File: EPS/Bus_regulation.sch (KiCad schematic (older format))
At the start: 1 part

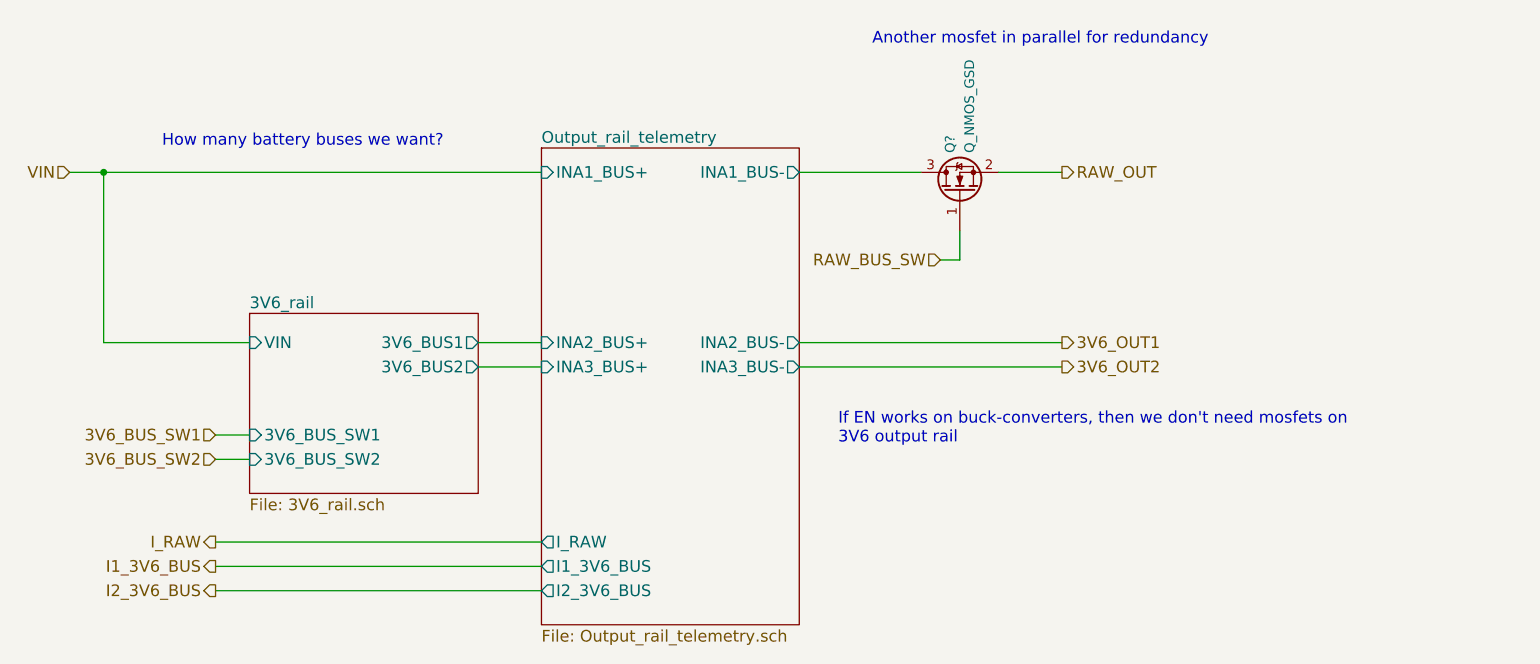
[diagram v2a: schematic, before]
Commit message: Finalized SCH (beta version) and started pcb
Capacitor banks might need to be reassigned to other locations.
No RBF pin on this SCH or PCB.
Battery gound deployment switch is fully mechanical (no mosfet switch on low side).
PCB of the prototype started. Main power converters and current measuring devices layed out.
SCH still requires ESD protection diodes!
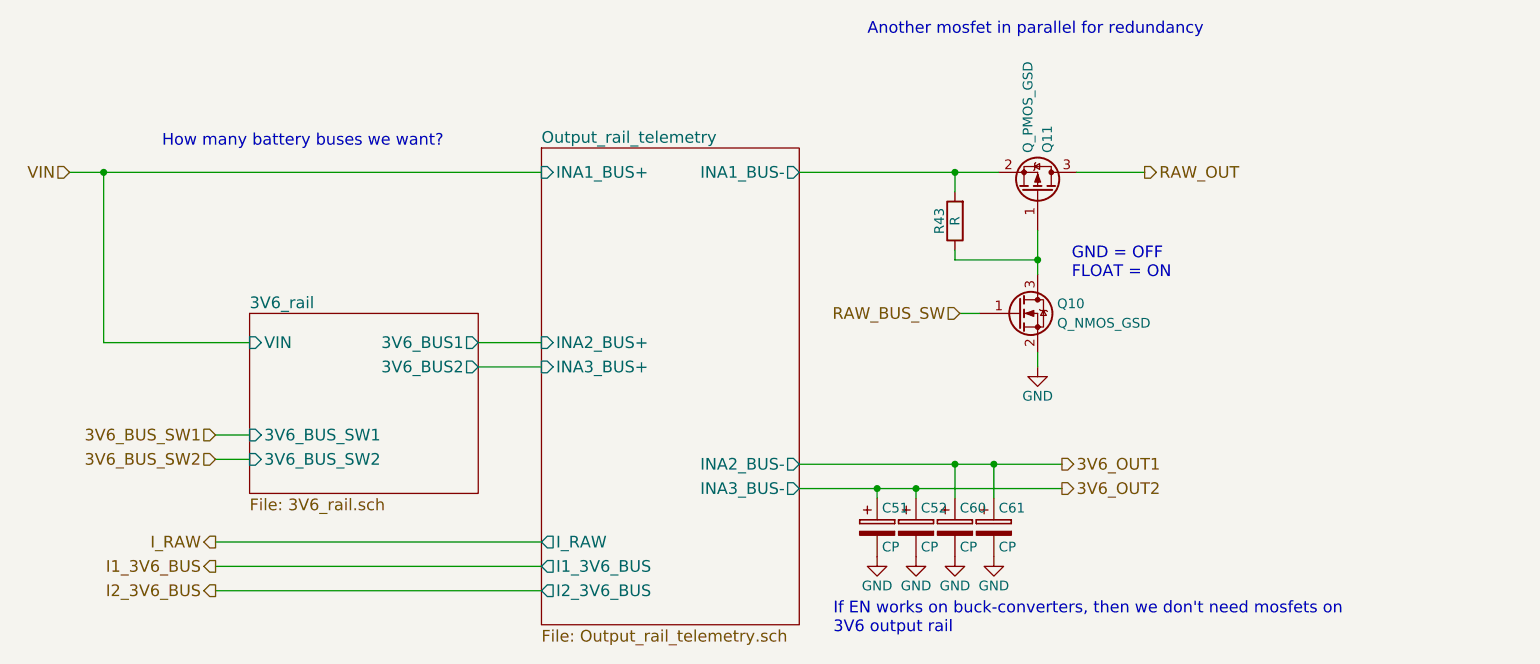
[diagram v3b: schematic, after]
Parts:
- removed Q?: Q_NMOS_GSD, symbol Q_NMOS_GSD
- added C51, C52, C60, C61: CP, Capacitors_Tantalum_SMD:CP_Tantalum_Case-C_EIA-6032-28_Reflow, symbol CP
- added Q10: Q_NMOS_GSD, TO_SOT_Packages_SMD:SOT-23, symbol Q_NMOS_GSD
- added Q11: Q_PMOS_GSD, TO_SOT_Packages_SMD:SOT-23, symbol Q_PMOS_GSD
- added R43: R, Resistors_SMD:R_0603, symbol R
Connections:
- net 3V6_OUT1: now also C60.1, C61.1
- net 3V6_OUT2: now also C51.1, C52.1
- net Output_rail_telemetry/INA1_BUS-: now also Q11.2 (S), R43.2
- net RAW_BUS_SW: now also Q10.1 (G)
- net RAW_OUT: now also Q11.3 (D)
- new net: Q10.3 (D), Q11.1 (G), R43.1
- new net GND: C51.2, C52.2, C60.2, C61.2, Q10.2 (S)
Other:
- note added: "GND = OFF\nFLOAT = ON"
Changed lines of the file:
@@
 $Descr A4 11693 8268
 encoding utf-8
-Sheet 10 14
+Sheet 9 14
 Title "Output regulation"
-Date "2018-02-15"
+Date "2018-02-22"
 Rev "R1"
 Comp ""
@@
 Text HLabel 3925 3725 0    60   Input ~ 0
 3V6_BUS_SW1
-Wire Wire Line
-	3925 3725 4100 3725
 Text HLabel 3925 3850 0    60   Input ~ 0
 3V6_BUS_SW2
-Wire Wire Line
-	3925 3850 4100 3850
 $Sheet
 S 5600 2250 1325 2450
@@
 F5 "I1_3V6_BUS" O L 5600 4400 60
 F6 "INA2_BUS+" I L 5600 3250 60
-F7 "INA2_BUS-" O R 6925 3250 60
-F8 "INA3_BUS-" O R 6925 3375 60
+F7 "INA2_BUS-" O R 6925 3875 60
+F8 "INA3_BUS-" O R 6925 4000 60
 F9 "INA3_BUS+" I L 5600 3375 60
 F10 "I2_3V6_BUS" O L 5600 4525 60
 $EndSheet
-Wire Wire Line
-	5600 2375 3175 2375
-Wire Wire Line
-	3350 2375 3350 3250
-Wire Wire Line
-	3350 3250 4100 3250
-Connection ~ 3350 2375
-Wire Wire Line
-	5275 3250 5600 3250
-Wire Wire Line
-	5275 3375 5600 3375
 Text HLabel 3925 4275 0    60   Output ~ 0
 I_RAW
-Wire Wire Line
-	3925 4275 5600 4275
 Text HLabel 3925 4400 0    60   Output ~ 0
 I1_3V6_BUS
-Wire Wire Line
-	3925 4400 5600 4400
 Text HLabel 3925 4525 0    60   Output ~ 0
 I2_3V6_BUS
-Wire Wire Line
-	3925 4525 5600 4525
-$Comp
-L Q_NMOS_GSD Q?
-U 1 1 5A9C3DA7
-P 7750 2475
-F 0 "Q?" H 7950 2525 50  0000 L CNN
-F 1 "Q_NMOS_GSD" H 7950 2425 50  0000 L CNN
-F 2 "" H 7950 2575 50  0001 C CNN
-F 3 "" H 7750 2475 50  0001 C CNN
-	1    7750 2475
-	0    -1   -1   0
-$EndComp
-Wire Wire Line
-	7550 2375 6925 2375
-Text HLabel 8275 2375 2    60   Output ~ 0
+Text HLabel 8700 2375 2    60   Output ~ 0
 RAW_OUT
-Wire Wire Line
-	8275 2375 7950 2375
-Text HLabel 8275 3250 2    60   Output ~ 0
+Text HLabel 8275 3875 2    60   Output ~ 0
 3V6_OUT1
-Text HLabel 8275 3375 2    60   Output ~ 0
+Text HLabel 8275 4000 2    60   Output ~ 0
 3V6_OUT2
-Wire Wire Line
-	8275 3375 6925 3375
-Wire Wire Line
-	6925 3250 8275 3250
-Text HLabel 7650 2825 0    60   Input ~ 0
+Text HLabel 7750 3100 0    60   Input ~ 0
 RAW_BUS_SW
-Wire Wire Line
-	7650 2825 7750 2825
-Wire Wire Line
-	7750 2825 7750 2675
-Text Notes 7125 3775 0    60   ~ 0
+Text Notes 7100 4750 0    60   ~ 0
 If EN works on buck-converters, then we don't need mosfets on\n3V6 output rail
-Text Notes 7300 1725 0    60   ~ 0
+Text Notes 7275 1675 0    60   ~ 0
 Another mosfet in parallel for redundancy
 Text Notes 3650 2250 0    60   ~ 0
 How many battery buses we want?
+$Comp
+L R R43
+U 1 1 5A9F980B
+P 7725 2625
+F 0 "R43" V 7805 2625 50  0000 C CNN
+F 1 "R" V 7725 2625 50  0000 C CNN
+F 2 "Resistors_SMD:R_0603" V 7655 2625 50  0001 C CNN
+F 3 "" H 7725 2625 50  0001 C CNN
+	1    7725 2625
+	-1   0    0    1
+$EndComp
+$Comp
+L Q_NMOS_GSD Q10
+U 1 1 5A9F9825
+P 8050 3100
+F 0 "Q10" H 8250 3150 50  0000 L CNN
+F 1 "Q_NMOS_GSD" H 8250 3050 50  0000 L CNN
+F 2 "TO_SOT_Packages_SMD:SOT-23" H 8250 3200 50  0001 C CNN
+F 3 "" H 8050 3100 50  0001 C CNN
+	1    8050 3100
+	1    0    0    -1
+$EndComp
+$Comp
+L GND #PWR0110
+U 1 1 5A9F982C
+P 8150 3375
+F 0 "#PWR0110" H 8150 3125 50  0001 C CNN
+F 1 "GND" H 8150 3225 50  0000 C CNN
+F 2 "" H 8150 3375 50  0001 C CNN
+F 3 "" H 8150 3375 50  0001 C CNN
+	1    8150 3375
+	1    0    0    -1
+$EndComp
+Text Notes 8325 2925 0    60   ~ 0
+GND = OFF\nFLOAT = ON
+$Comp
+L Q_PMOS_GSD Q11
+U 1 1 5A9FD422
+P 8150 2475
+F 0 "Q11" H 8350 2525 50  0000 L CNN
+F 1 "Q_PMOS_GSD" H 8350 2425 50  0000 L CNN
+F 2 "TO_SOT_Packages_SMD:SOT-23" H 8350 2575 50  0001 C CNN
+F 3 "" H 8150 2475 50  0001 C CNN
+	1    8150 2475
+	0    1    -1   0
+$EndComp
+Wire Wire Line
+	3925 3725 4100 3725
+Wire Wire Line
+	3925 3850 4100 3850
+Wire Wire Line
+	3175 2375 5600 2375
+Wire Wire Line
+	3350 2375 3350 3250
+Wire Wire Line
+	3350 3250 4100 3250
+Connection ~ 3350 2375
+Wire Wire Line
+	5275 3250 5600 3250
+Wire Wire Line
+	5275 3375 5600 3375
+Wire Wire Line
+	3925 4275 5600 4275
+Wire Wire Line
+	3925 4400 5600 4400
+Wire Wire Line
+	3925 4525 5600 4525
+Wire Wire Line
+	6925 2375 7950 2375
+Wire Wire Line
+	8350 2375 8700 2375
+Wire Wire Line
+	7725 2475 7725 2375
+Connection ~ 7725 2375
+Wire Wire Line
+	7725 2775 7725 2825
+Wire Wire Line
+	7725 2825 8150 2825
+Wire Wire Line
+	8150 2675 8150 2900
+Connection ~ 8150 2825
+Wire Wire Line
+	8150 3375 8150 3300
+Wire Wire Line
+	7850 3100 7750 3100
+Wire Wire Line
+	6925 3875 8275 3875
+Wire Wire Line
+	8275 4000 6925 4000
+$Comp
+L CP C52
+U 1 1 5A96ADC2
+P 7525 4200
+F 0 "C52" H 7550 4300 50  0000 L CNN
+F 1 "CP" H 7550 4100 50  0000 L CNN
+F 2 "Capacitors_Tantalum_SMD:CP_Tantalum_Case-C_EIA-6032-28_Reflow" H 7563 4050 50  0001 C CNN
+F 3 "" H 7525 4200 50  0001 C CNN
+	1    7525 4200
+	1    0    0    -1
+$EndComp
+$Comp
+L CP C51
+U 1 1 5A96AE4D
+P 7325 4200
+F 0 "C51" H 7350 4300 50  0000 L CNN
+F 1 "CP" H 7350 4100 50  0000 L CNN
+F 2 "Capacitors_Tantalum_SMD:CP_Tantalum_Case-C_EIA-6032-28_Reflow" H 7363 4050 50  0001 C CNN
+F 3 "" H 7325 4200 50  0001 C CNN
+	1    7325 4200
+	1    0    0    -1
+$EndComp
+$Comp
+L CP C60
+U 1 1 5A96AF69
+P 7725 4200
+F 0 "C60" H 7750 4300 50  0000 L CNN
+F 1 "CP" H 7750 4100 50  0000 L CNN
+F 2 "Capacitors_Tantalum_SMD:CP_Tantalum_Case-C_EIA-6032-28_Reflow" H 7763 4050 50  0001 C CNN
+F 3 "" H 7725 4200 50  0001 C CNN
+	1    7725 4200
+	1    0    0    -1
+$EndComp
+$Comp
+L CP C61
+U 1 1 5A96AFE3
+P 7925 4200
+F 0 "C61" H 7950 4300 50  0000 L CNN
+F 1 "CP" H 7950 4100 50  0000 L CNN
+F 2 "Capacitors_Tantalum_SMD:CP_Tantalum_Case-C_EIA-6032-28_Reflow" H 7963 4050 50  0001 C CNN
+F 3 "" H 7925 4200 50  0001 C CNN
+	1    7925 4200
+	1    0    0    -1
+$EndComp
+Wire Wire Line
+	7925 4050 7925 3875
+Connection ~ 7925 3875
+Wire Wire Line
+	7725 4050 7725 3875
+Connection ~ 7725 3875
+Wire Wire Line
+	7525 4050 7525 4000
+Connection ~ 7525 4000
+Wire Wire Line
+	7325 4050 7325 4000
+Connection ~ 7325 4000
+$Comp
+L GND #PWR0111
+U 1 1 5A96B19C
+P 7325 4350
+F 0 "#PWR0111" H 7325 4100 50  0001 C CNN
+F 1 "GND" H 7325 4200 50  0000 C CNN
+F 2 "" H 7325 4350 50  0001 C CNN
+F 3 "" H 7325 4350 50  0001 C CNN
+	1    7325 4350
+	1    0    0    -1
+$EndComp
+$Comp
+L GND #PWR0112
+U 1 1 5A96B210
+P 7525 4350
+F 0 "#PWR0112" H 7525 4100 50  0001 C CNN
+F 1 "GND" H 7525 4200 50  0000 C CNN
+F 2 "" H 7525 4350 50  0001 C CNN
+F 3 "" H 7525 4350 50  0001 C CNN
+	1    7525 4350
+	1    0    0    -1
+$EndComp
+$Comp
+L GND #PWR0113
+U 1 1 5A96B284
+P 7725 4350
+F 0 "#PWR0113" H 7725 4100 50  0001 C CNN
+F 1 "GND" H 7725 4200 50  0000 C CNN
+F 2 "" H 7725 4350 50  0001 C CNN
+F 3 "" H 7725 4350 50  0001 C CNN
+	1    7725 4350
+	1    0    0    -1
+$EndComp
+$Comp
+L GND #PWR0114
+U 1 1 5A96B2F8
+P 7925 4350
+F 0 "#PWR0114" H 7925 4100 50  0001 C CNN
+F 1 "GND" H 7925 4200 50  0000 C CNN
+F 2 "" H 7925 4350 50  0001 C CNN
+F 3 "" H 7925 4350 50  0001 C CNN
+	1    7925 4350
+	1    0    0    -1
+$EndComp
 $EndSCHEMATC
